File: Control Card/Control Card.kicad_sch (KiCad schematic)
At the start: 13 parts, among them Q1 2N7002, Q2 2N7002

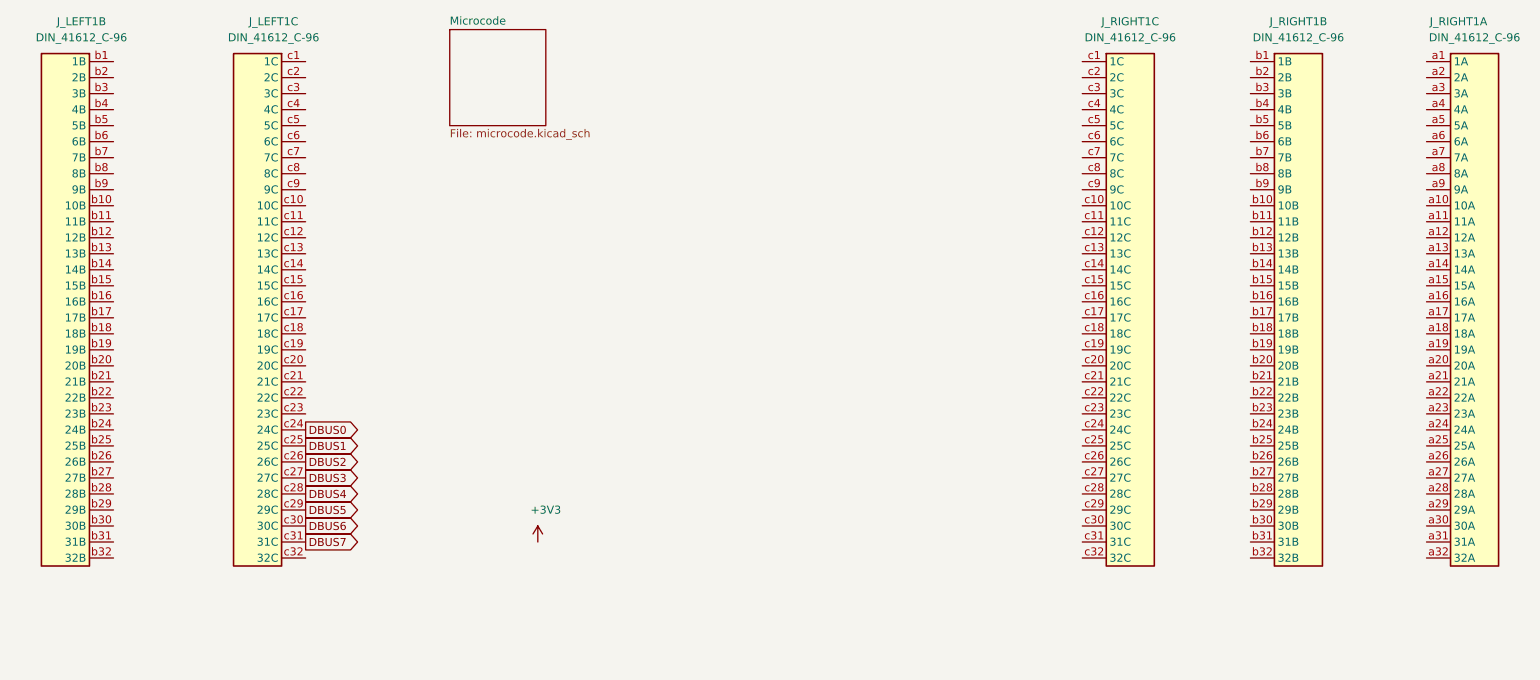
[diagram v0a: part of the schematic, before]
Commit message: add lots of nets to the Din connectors
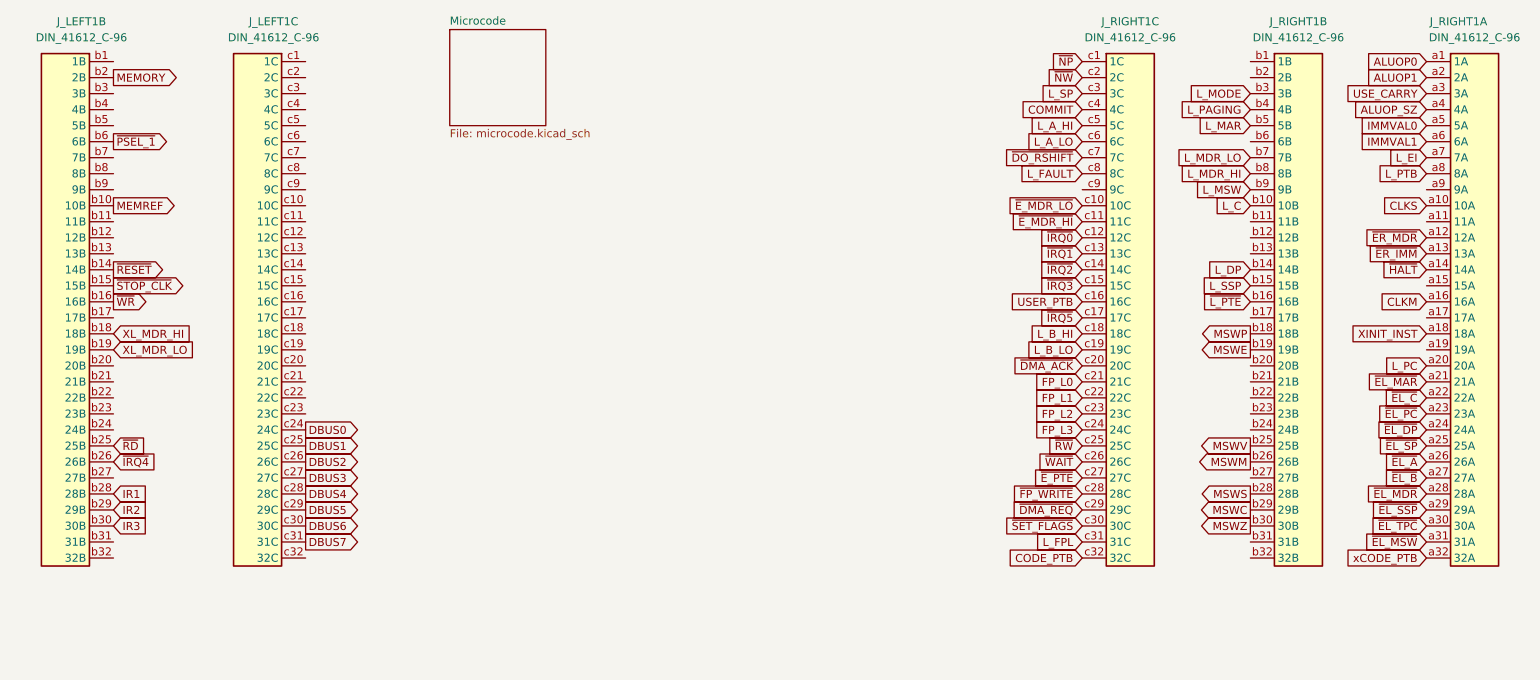
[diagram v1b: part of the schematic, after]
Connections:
- net MEMREF: now reaches J_LEFT1.b10 (10B)
- net ~RESET~: now reaches J_LEFT1.b14 (14B)
- net ~STOP_CLK~: now reaches J_LEFT1.b15 (15B)
- net ~WR~: now reaches J_LEFT1.b16 (16B)
- net XL_MDR_HI: now reaches J_LEFT1.b18 (18B)
- net XL_MDR_LO: now reaches J_LEFT1.b19 (19B)
- net MEMORY: now reaches J_LEFT1.b2 (2B)
- net ~RD~: now reaches J_LEFT1.b25 (25B)
- net ~IRQ4~: now reaches J_LEFT1.b26 (26B)
- net IR1: now reaches J_LEFT1.b28 (28B)
- net IR2: now reaches J_LEFT1.b29 (29B)
- net IR3: now reaches J_LEFT1.b30 (30B)
- net ~PSEL_1~: now reaches J_LEFT1.b6 (6B)
- net L_C: now reaches J_RIGHT1.b10 (10B)
- net L_DP: now reaches J_RIGHT1.b14 (14B)
- net L_SSP: now reaches J_RIGHT1.b15 (15B)
- net ~L_PTE~: now reaches J_RIGHT1.b16 (16B)
- net MSWP: now reaches J_RIGHT1.b18 (18B)
- net MSWE: now reaches J_RIGHT1.b19 (19B)
- net MSWV: now reaches J_RIGHT1.b25 (25B)
- net MSWM: now reaches J_RIGHT1.b26 (26B)
- net MSWS: now reaches J_RIGHT1.b28 (28B)
- net MSWC: now reaches J_RIGHT1.b29 (29B)
- net L_MODE: now reaches J_RIGHT1.b3 (3B)
- net MSWZ: now reaches J_RIGHT1.b30 (30B)
- net L_PAGING: now reaches J_RIGHT1.b4 (4B)
- net L_MAR: now reaches J_RIGHT1.b5 (5B)
- net L_MDR_LO: now reaches J_RIGHT1.b7 (7B)
- net L_MDR_HI: now reaches J_RIGHT1.b8 (8B)
- net L_MSW: now reaches J_RIGHT1.b9 (9B)
- net ALUOP0: now reaches J_RIGHT1.a1 (1A)
- net CLKS: now reaches J_RIGHT1.a10 (10A)
- net ~ER_MDR~: now reaches J_RIGHT1.a12 (12A)
- net ~ER_IMM~: now reaches J_RIGHT1.a13 (13A)
- net ~HALT~: now reaches J_RIGHT1.a14 (14A)
- net CLKM: now reaches J_RIGHT1.a16 (16A)
- net XINIT_INST: now reaches J_RIGHT1.a18 (18A)
- net ALUOP1: now reaches J_RIGHT1.a2 (2A)
- net L_PC: now reaches J_RIGHT1.a20 (20A)
- net ~EL_MAR~: now reaches J_RIGHT1.a21 (21A)
- net ~EL_C~: now reaches J_RIGHT1.a22 (22A)
- net ~EL_PC~: now reaches J_RIGHT1.a23 (23A)
- net ~EL_DP~: now reaches J_RIGHT1.a24 (24A)
- net ~EL_SP~: now reaches J_RIGHT1.a25 (25A)
- net ~EL_A~: now reaches J_RIGHT1.a26 (26A)
- net ~EL_B~: now reaches J_RIGHT1.a27 (27A)
- net ~EL_MDR~: now reaches J_RIGHT1.a28 (28A)
- net ~EL_SSP~: now reaches J_RIGHT1.a29 (29A)
- net USE_CARRY: now reaches J_RIGHT1.a3 (3A)
- net ~EL_TPC~: now reaches J_RIGHT1.a30 (30A)
- net ~EL_MSW~: now reaches J_RIGHT1.a31 (31A)
- net xCODE_PTB: now reaches J_RIGHT1.a32 (32A)
- net ALUOP_SZ: now reaches J_RIGHT1.a4 (4A)
- net IMMVAL0: now reaches J_RIGHT1.a5 (5A)
- net IMMVAL1: now reaches J_RIGHT1.a6 (6A)
- net L_EI: now reaches J_RIGHT1.a7 (7A)
- net L_PTB: now reaches J_RIGHT1.a8 (8A)
- net ~NP~: now reaches J_RIGHT1.c1 (1C)
- net ~E_MDR_LO~: now reaches J_RIGHT1.c10 (10C)
- net ~E_MDR_HI~: now reaches J_RIGHT1.c11 (11C)
- net ~IRQ0~: now reaches J_RIGHT1.c12 (12C)
- net ~IRQ1~: now reaches J_RIGHT1.c13 (13C)
- net ~IRQ2~: now reaches J_RIGHT1.c14 (14C)
- net ~IRQ3~: now reaches J_RIGHT1.c15 (15C)
- net USER_PTB: now reaches J_RIGHT1.c16 (16C)
- net ~IRQ5~: now reaches J_RIGHT1.c17 (17C)
- net L_B_HI: now reaches J_RIGHT1.c18 (18C)
- net L_B_LO: now reaches J_RIGHT1.c19 (19C)
- net ~NW~: now reaches J_RIGHT1.c2 (2C)
- net ~DMA_ACK~: now reaches J_RIGHT1.c20 (20C)
- net FP_L0: now reaches J_RIGHT1.c21 (21C)
- net FP_L1: now reaches J_RIGHT1.c22 (22C)
- net FP_L2: now reaches J_RIGHT1.c23 (23C)
- net FP_L3: now reaches J_RIGHT1.c24 (24C)
- net ~RW~: now reaches J_RIGHT1.c25 (25C)
- net ~WAIT~: now reaches J_RIGHT1.c26 (26C)
- net ~E_PTE~: now reaches J_RIGHT1.c27 (27C)
- net ~FP_WRITE~: now reaches J_RIGHT1.c28 (28C)
- net ~DMA_REQ~: now reaches J_RIGHT1.c29 (29C)
- net L_SP: now reaches J_RIGHT1.c3 (3C)
- net ~SET_FLAGS~: now reaches J_RIGHT1.c30 (30C)
- net L_FPL: now reaches J_RIGHT1.c31 (31C)
- net CODE_PTB: now reaches J_RIGHT1.c32 (32C)
- net COMMIT: now reaches J_RIGHT1.c4 (4C)
- net L_A_HI: now reaches J_RIGHT1.c5 (5C)
- net L_A_LO: now reaches J_RIGHT1.c6 (6C)
- net ~DO_RSHIFT~: now reaches J_RIGHT1.c7 (7C)
- net L_FAULT: now reaches J_RIGHT1.c8 (8C)
